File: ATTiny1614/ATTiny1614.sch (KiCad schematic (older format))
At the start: 22 parts, among them J1 Conn_01x07, J2 Conn_01x02, J3 Conn_01x07, J4 ISP6, SW1 RST, U1 AP2204K-ADJ, U2 ATtiny1614-SS

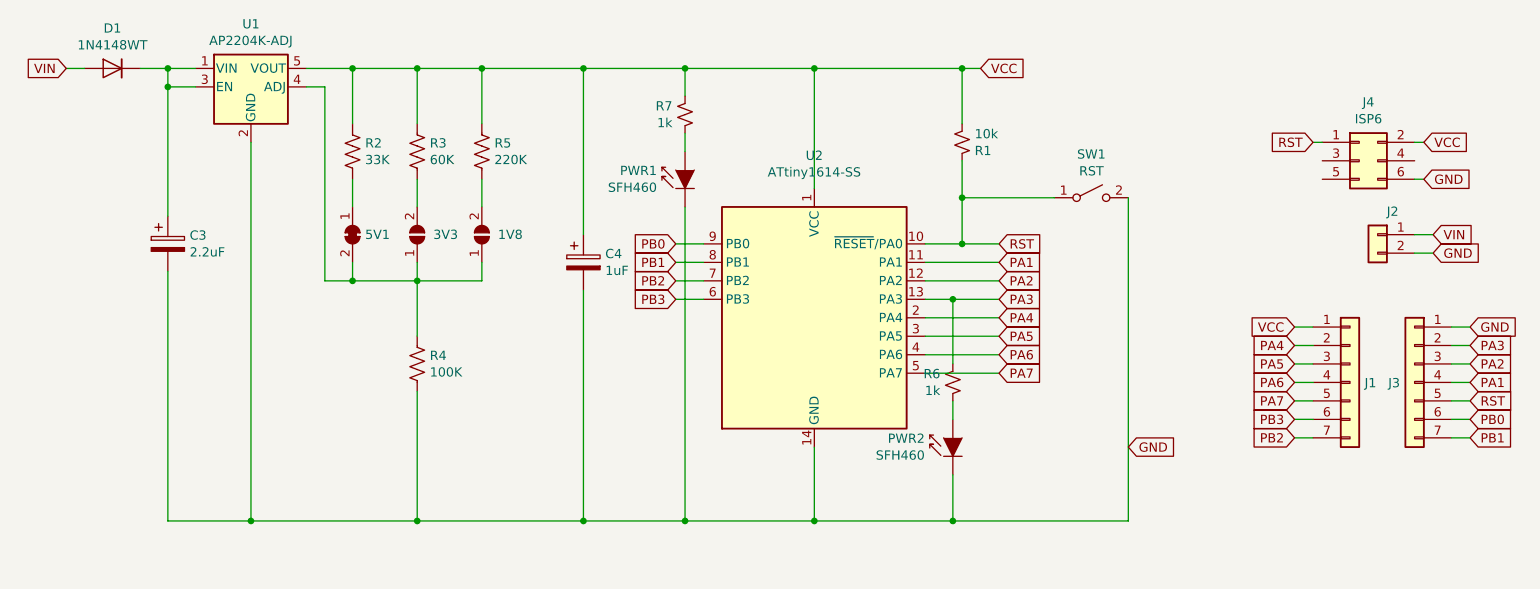
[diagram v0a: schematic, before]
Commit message: Silkscreens Orientated
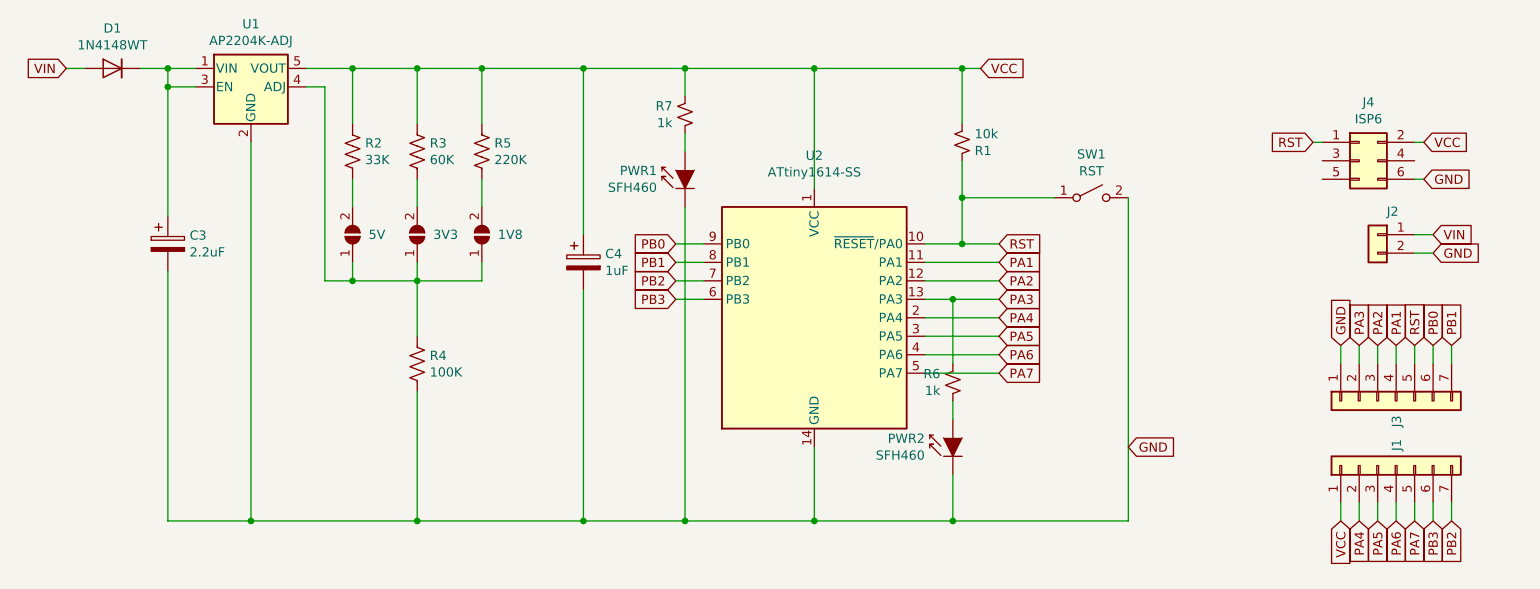
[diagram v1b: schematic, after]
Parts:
- removed 5V1: SolderJumper_2_Bridged, Jumper:SolderJumper-2_P1.3mm_Bridged_RoundedPad1.0x1.5mm, symbol Jumper:SolderJumper_2_Bridged
- added 5V: SolderJumper_2_Open, Jumper:SolderJumper-2_P1.3mm_Open_RoundedPad1.0x1.5mm, symbol Jumper:SolderJumper_2_Open
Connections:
- net at R2.2: now also 5V.2 (B)
- net at 1V8.1 (A), 3V3.1 (A), R4.1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: now also 5V.1 (A)
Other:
- moved on the sheet: J1, J3
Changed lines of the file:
@@
 	1    0    0    -1
 $EndComp
-Text GLabel 9650 4250 0    50   Input ~ 0
+Text GLabel 9900 5300 3    50   Input ~ 0
 VCC
 Text GLabel 7950 2850 2    50   Input ~ 0
@@
 Text GLabel 10400 3750 2    50   Input ~ 0
 VIN
-Text GLabel 10600 4250 2    50   Input ~ 0
+Text GLabel 9900 4350 1    50   Input ~ 0
 GND
 Wire Wire Line
-	10500 4250 10600 4250
+	9900 4450 9900 4350
 Wire Wire Line
 	10400 3750 10300 3750
@@
 	3550 2850 3700 2850
 Wire Wire Line
-	9750 4250 9650 4250
-Wire Wire Line
-	10600 4350 10500 4350
-Wire Wire Line
-	10500 4650 10600 4650
-Wire Wire Line
-	10600 4450 10500 4450
+	9900 5200 9900 5300
+Wire Wire Line
+	10000 4350 10000 4450
+Wire Wire Line
+	10300 4450 10300 4350
+Wire Wire Line
+	10100 4350 10100 4450
 Text GLabel 8050 4100 2    50   Input ~ 0
 PA3
@@
 Wire Wire Line
 	6350 3000 6350 2850
-Text GLabel 10600 4650 2    50   Input ~ 0
+Text GLabel 10300 4350 1    50   Input ~ 0
 RST
-Text GLabel 10600 4450 2    50   Input ~ 0
+Text GLabel 10100 4350 1    50   Input ~ 0
 PA2
-Text GLabel 10600 4350 2    50   Input ~ 0
+Text GLabel 10000 4350 1    50   Input ~ 0
 PA3
 Connection ~ 6350 2850
@@
 Wire Wire Line
 	4300 2950 4400 2950
-$Comp
-L Jumper:SolderJumper_2_Bridged 5V1
-U 1 1 5D4D08FE
-P 4550 3750
-F 0 "5V1" V 4550 3818 50  0000 L CNN
-F 1 "SolderJumper_2_Bridged" V 4595 3818 50  0001 L CNN
-F 2 "Jumper:SolderJumper-2_P1.3mm_Bridged_RoundedPad1.0x1.5mm" H 4550 3750 50  0001 C CNN
-F 3 "~" H 4550 3750 50  0001 C CNN
-	1    4550 3750
-	0    1    1    0
-$EndComp
 Wire Wire Line
 	5250 3450 5250 3600
@@
 	6450 4100 6300 4100
 Wire Wire Line
-	10600 4550 10500 4550
-Text GLabel 10600 4550 2    50   Input ~ 0
+	10200 4350 10200 4450
+Text GLabel 10200 4350 1    50   Input ~ 0
 PA1
-Text GLabel 10600 4850 2    50   Input ~ 0
+Text GLabel 10500 4350 1    50   Input ~ 0
 PB1
-Text GLabel 10600 4750 2    50   Input ~ 0
+Text GLabel 10400 4350 1    50   Input ~ 0
 PB0
 Wire Wire Line
-	10600 4750 10500 4750
-Wire Wire Line
-	10500 4850 10600 4850
-Wire Wire Line
-	9750 4750 9650 4750
-Wire Wire Line
-	9650 4850 9750 4850
-Text GLabel 9650 4750 0    50   Input ~ 0
+	10400 4350 10400 4450
+Wire Wire Line
+	10500 4450 10500 4350
+Wire Wire Line
+	10400 5200 10400 5300
+Wire Wire Line
+	10500 5300 10500 5200
+Text GLabel 10400 5300 3    50   Input ~ 0
 PB3
-Text GLabel 9650 4850 0    50   Input ~ 0
+Text GLabel 10500 5300 3    50   Input ~ 0
 PB2
 Wire Wire Line
-	9650 4450 9750 4450
-Wire Wire Line
-	9750 4350 9650 4350
-Text GLabel 9650 4350 0    50   Input ~ 0
+	10100 5300 10100 5200
+Wire Wire Line
+	10000 5200 10000 5300
+Text GLabel 10000 5300 3    50   Input ~ 0
 PA4
-Text GLabel 9650 4450 0    50   Input ~ 0
+Text GLabel 10100 5300 3    50   Input ~ 0
 PA5
 Wire Wire Line
-	9750 4550 9650 4550
-Wire Wire Line
-	9750 4650 9650 4650
-Text GLabel 9650 4550 0    50   Input ~ 0
+	10200 5200 10200 5300
+Wire Wire Line
+	10300 5200 10300 5300
+Text GLabel 10200 5300 3    50   Input ~ 0
 PA6
-Text GLabel 9650 4650 0    50   Input ~ 0
+Text GLabel 10300 5300 3    50   Input ~ 0
 PA7
 $Comp
 L Connector_Generic:Conn_01x07 J1
 U 1 1 5D3FB5C9
-P 9950 4550
-F 0 "J1" H 10029 4547 50  0000 L CNN
-F 1 "Conn_01x07" H 10029 4502 50  0001 L CNN
-F 2 "Connector_PinHeader_2.54mm:PinHeader_1x07_P2.54mm_Vertical" H 9950 4550 50  0001 C CNN
-F 3 "~" H 9950 4550 50  0001 C CNN
-	1    9950 4550
-	1    0    0    -1
+P 10200 5000
+F 0 "J1" H 10279 4997 50  0000 L CNN
+F 1 "Conn_01x07" H 10279 4952 50  0001 L CNN
+F 2 "Connector_PinHeader_2.54mm:PinHeader_1x07_P2.54mm_Vertical" H 10200 5000 50  0001 C CNN
+F 3 "~" H 10200 5000 50  0001 C CNN
+	1    10200 5000
+	0    -1   -1   0
 $EndComp
 $Comp
 L Connector_Generic:Conn_01x07 J3
 U 1 1 5D3FEBC4
-P 10300 4550
-F 0 "J3" H 10379 4547 50  0000 L CNN
-F 1 "Conn_01x07" H 10379 4502 50  0001 L CNN
-F 2 "Connector_PinHeader_2.54mm:PinHeader_1x07_P2.54mm_Vertical" H 10300 4550 50  0001 C CNN
-F 3 "~" H 10300 4550 50  0001 C CNN
-	1    10300 4550
-	-1   0    0    -1
+P 10200 4650
+F 0 "J3" H 10279 4647 50  0000 L CNN
+F 1 "Conn_01x07" H 10279 4602 50  0001 L CNN
+F 2 "Connector_PinHeader_2.54mm:PinHeader_1x07_P2.54mm_Vertical" H 10200 4650 50  0001 C CNN
+F 3 "~" H 10200 4650 50  0001 C CNN
+	1    10200 4650
+	0    -1   1    0
 $EndComp
 Wire Wire Line
@@
 Wire Wire Line
 	7800 4100 8050 4100
+$Comp
+L Jumper:SolderJumper_2_Open 5V
+U 1 1 5D608218
+P 4550 3750
+F 0 "5V" V 4550 3663 50  0000 R CNN
+F 1 "SolderJumper_2_Open" H 4550 3863 50  0001 C CNN
+F 2 "Jumper:SolderJumper-2_P1.3mm_Open_RoundedPad1.0x1.5mm" H 4550 3750 50  0001 C CNN
+F 3 "~" H 4550 3750 50  0001 C CNN
+	1    4550 3750
+	0    -1   -1   0
+$EndComp
 $EndSCHEMATC
